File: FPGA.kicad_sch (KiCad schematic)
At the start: 32 parts, among them IC5 AD817ARZ, IC8 N25Q032A11EF840, J3 Conn_01x02, J4 Conn_02x02_Top_Bottom, J5 Conn_01x02, U4 ICE5LP1K-SG48, U9 LTC2451xDDB

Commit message: Begun schematics
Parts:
- removed C20: CC0603_10UF_25V_20%_X5R, Capacitors SMD:CAPC1709X100N, symbol Capacitors SMD:CC0603_10UF_25V_20%_X5R
- removed C21: CC0603_100NF_50V_10%_X7R, Capacitors SMD:CAPC1608X87N, symbol Capacitors SMD:CC0603_100NF_50V_10%_X7R
- removed IC8: N25Q032A11EF840, ICs And Semiconductors SMD:SON127P800X600X100-9N-R515X480, symbol Logic:N25Q032A11EF840
- added D1 (x3): SMBJ3V3, ICs And Semiconductors SMD:DIOM5436X244N, symbol Diodes:SMBJ3V3
- added IC8: MT25QL128ABA1ESE-0SIT, ICs And Semiconductors SMD:SOIC127P790X216-8N, symbol Logic:MT25QL128ABA1ESE-0SIT
- added LD5: LED_LITEON_LTST-C193KGKT-5A, ICs And Semiconductors SMD:LED_LITEON_LTST-C193KGKT-5A, symbol LEDs & Displays:LED_LITEON_LTST-C193KGKT-5A
- added R15: R0603_2K2_1%_0.1W_100PPM, Resistors SMD:RESC1608X55N, symbol Resistors SMD:R0603_2K2_1%_0.1W_100PPM
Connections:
- net +3V3D: now also IC8.8 (VCC), R15.2; no longer C2.1
- net FLASH_MISO: now also IC8.2 (DQ1)
- net FLASH_MOSI: now also IC8.5 (DQ0)
- net GND: now also D1.2 (A), D1.2 (A), D1.2 (A), IC8.4 (VSS)
- net iCE_CDONE: now also D1.1 (C)
- net iCE_SCK: now also IC8.6 (C)
- net iCE_SS_B: now also D1.1 (C)
- net at J3.1 (Pin_1), R25.1: now also D1.1 (C), IC8.1 (~{S})
- net at R24.1: now also IC8.7 (~{HOLD/}DQ3)
- net at R23.1: now also IC8.3 (~{W/}DQ2)
- net +2V5: now reaches U4.24 (VPP_2V5)
- net +2V5: now also C2.1
- net +5VA renamed +5V
- new net: LD5.2 (A), R15.1
- new net FPGA_Alive: LD5.1 (C)
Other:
- moved on the sheet: C2, C20, C21, J3, LD1, R26, U4D

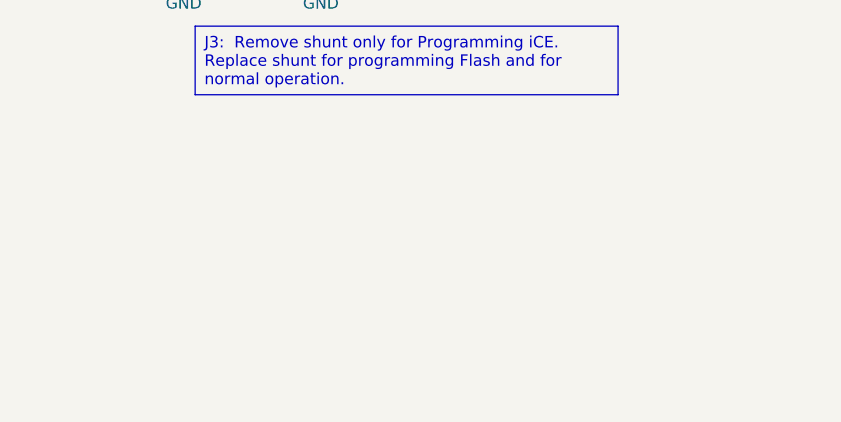
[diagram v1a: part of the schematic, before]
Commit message: Added FPGA oscillator, made FPGA sheet larger
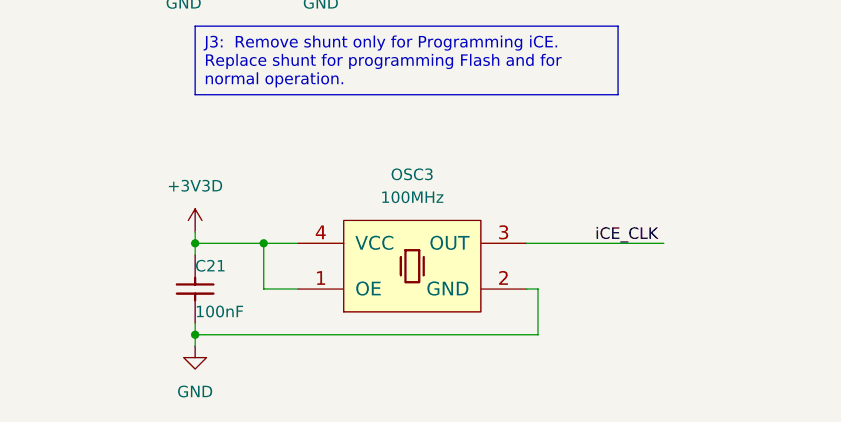
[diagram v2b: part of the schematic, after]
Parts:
- added C21: CC0603_100NF_50V_10%_X7R, Capacitors SMD:CAPC1608X87N, symbol Capacitors SMD:CC0603_100NF_50V_10%_X7R
- added OSC3: OSC_100MHZ_EPSON_SG-8002CAPCB100MHZ, ICs And Semiconductors SMD:OSC_EPSON_SG-8002CA, symbol Crystals & Oscillators:OSC_100MHZ_EPSON_SG-8002CAPCB100MHZ
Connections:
- net +3V3D: now also C21.1, OSC3.1 (OE), OSC3.4 (VCC)
- net GND: now also C21.2, OSC3.2 (GND)
- new net iCE_CLK: OSC3.3 (OUT)

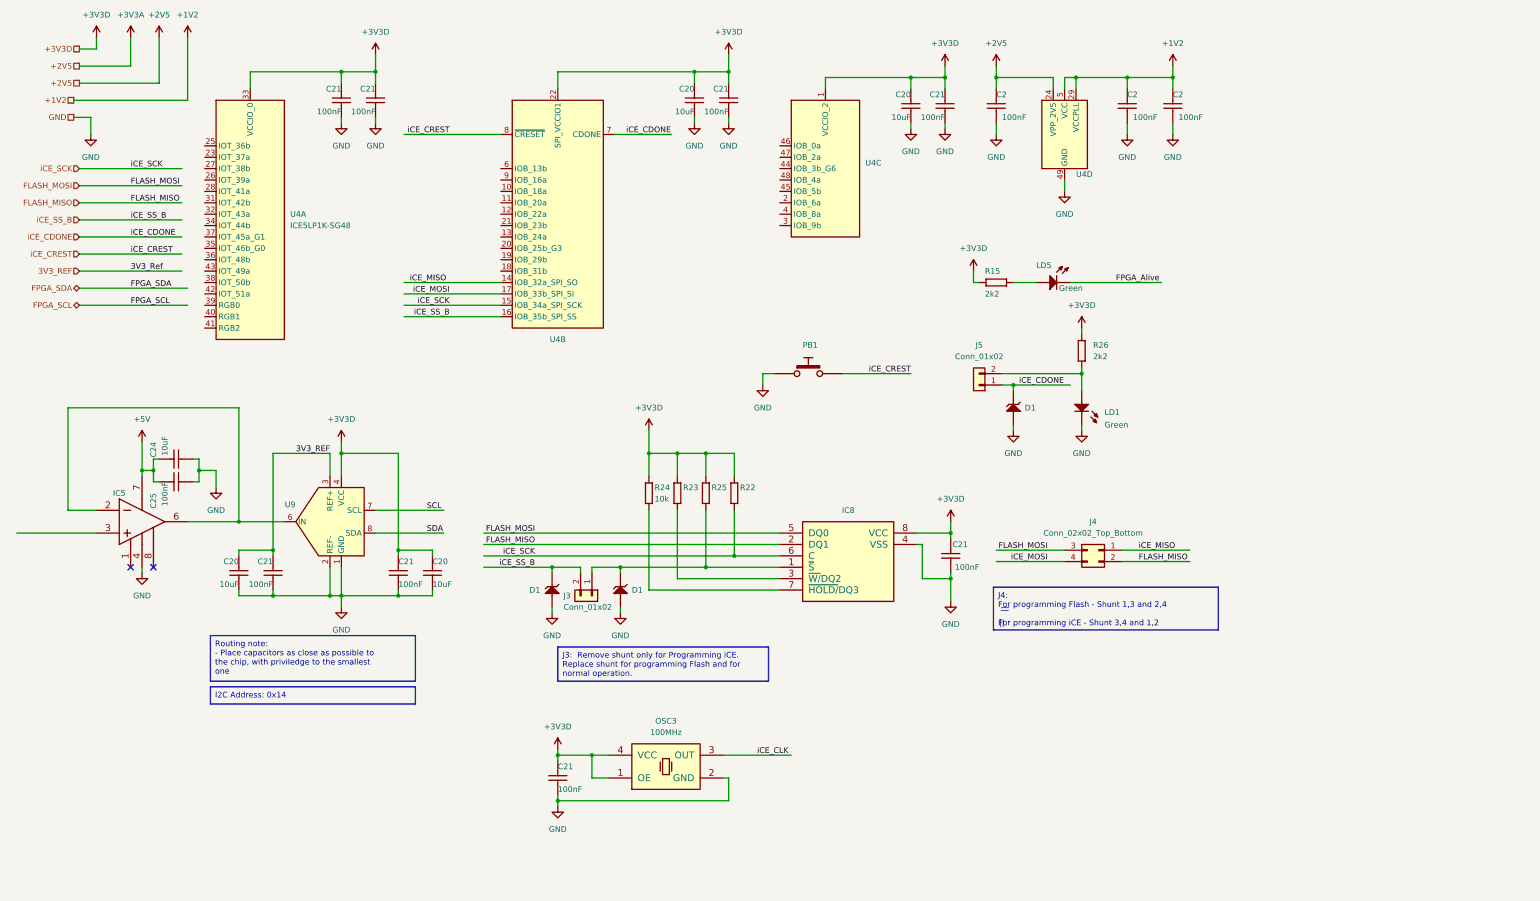
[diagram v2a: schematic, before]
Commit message: Connected FPGA to Accurate, added Atsam, fixed some Accurate connections
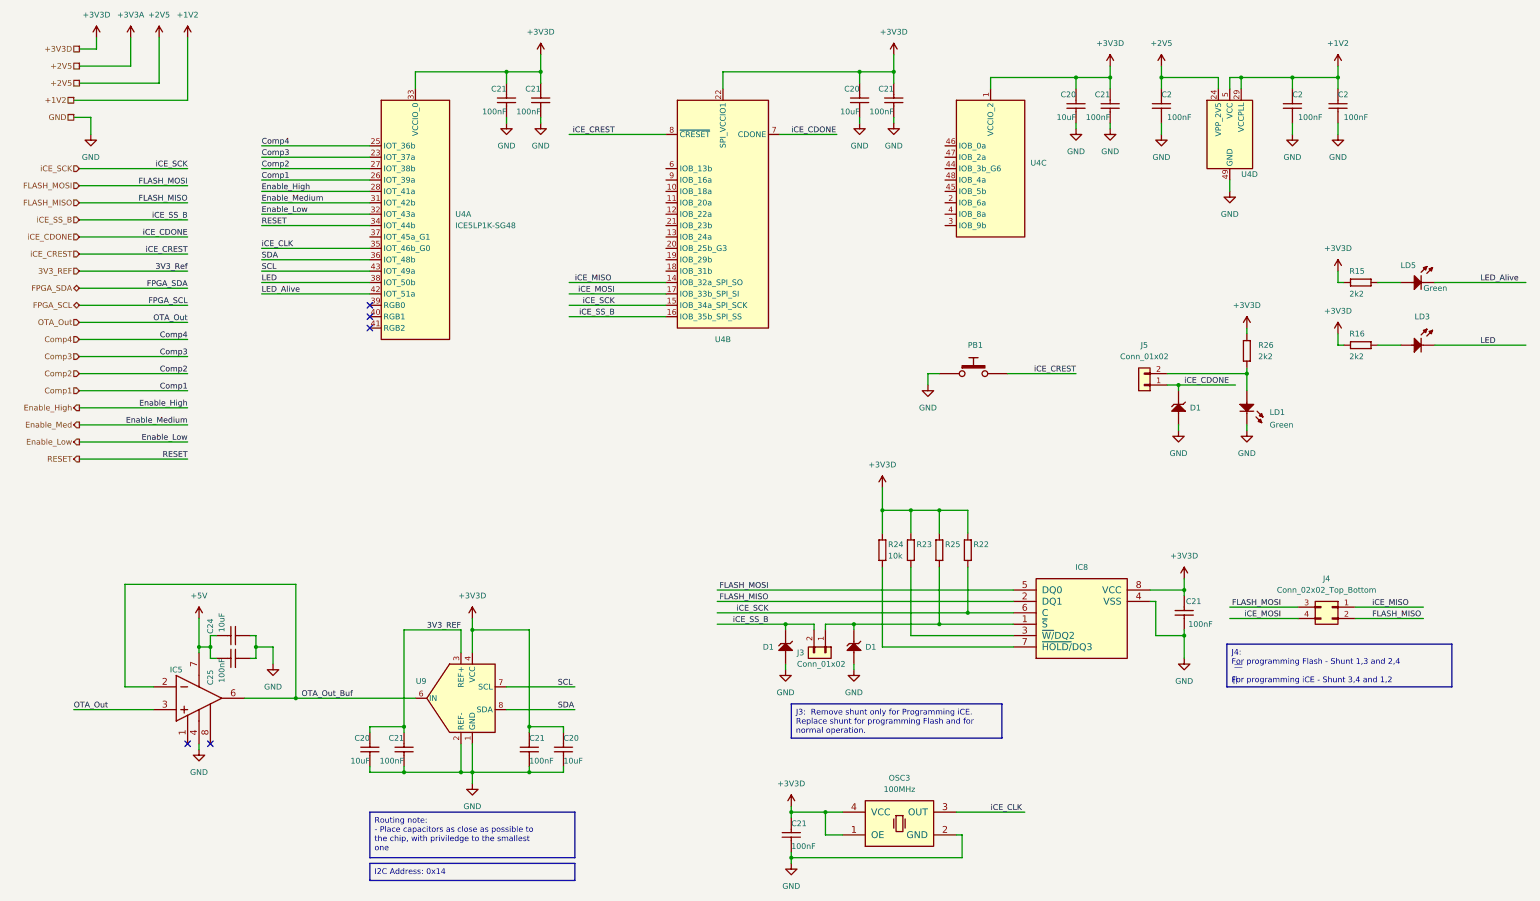
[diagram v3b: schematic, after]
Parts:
- added LD3: LED_LITEON_LTST-C193KSKT-5A, ICs And Semiconductors SMD:LED_LITEON_LTST-C193KSKT-5A, symbol LEDs & Displays:LED_LITEON_LTST-C193KSKT-5A
- added R16: R0603_2K2_1%_0.1W_100PPM, Resistors SMD:RESC1608X55N, symbol Resistors SMD:R0603_2K2_1%_0.1W_100PPM
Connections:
- net FPGA_Alive is gone; now on net LED_Alive: LD5.1 (C)
- net +3V3D: now also R16.2
- net SCL: now also U4.43 (IOT_49a)
- net SDA: now also U4.36 (IOT_48b)
- net iCE_CLK: now also U4.35 (IOT_46b_G0)
- net OTA_Out_Buf: now reaches IC5.2 (IN-), IC5.6 (OUT), U9.6 (IN)
- net Comp3: now reaches U4.23 (IOT_37a)
- net Comp4: now reaches U4.25 (IOT_36b)
- net Comp1: now reaches U4.26 (IOT_39a)
- net Comp2: now reaches U4.27 (IOT_38b)
- net Enable_High: now reaches U4.28 (IOT_41a)
- net Enable_Med: now reaches U4.31 (IOT_42b)
- net Enable_Low: now reaches U4.32 (IOT_43a)
- net RESET: now reaches U4.34 (IOT_44b)
- net LED: now reaches U4.38 (IOT_50b)
- net LED: now also LD3.1 (C)
- net LED_Alive: now reaches U4.42 (IOT_51a)
- net OTA_Out: now reaches IC5.3 (IN+)
- new net: LD3.2 (A), R16.1
- no-connect marks 2 -> 5
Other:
- moved on the sheet: C2, C20, C21, C24, C25, D1, IC5, IC8, J3, J4, J5, LD1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

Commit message: Made MCU schematic, made root schematic, adding ESD diodes, fixed  EDR errors
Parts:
- added C21 (x2): CC0603_100NF_50V_10%_X7R, Capacitors SMD:CAPC1608X87N, symbol Capacitors SMD:CC0603_100NF_50V_10%_X7R
- added D6: PESD3V3L5UY, Package_TO_SOT_SMD:SOT-363_SC-70-6, symbol Power_Protection:PESD3V3L5UY
- added J13, J8: Conn_02x06_Top_Bottom, symbol Connector_Generic:Conn_02x06_Top_Bottom
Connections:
- net SCL is gone; now on net FPGA_SCL: U4.43 (IOT_49a), U9.7 (SCL)
- net SDA is gone; now on net FPGA_SDA: U4.36 (IOT_48b), U9.8 (SDA)
- net +3V3D: now also C21.1, C21.1, J13.12 (Pin_12), J13.6 (Pin_6), J8.12 (Pin_12), J8.6 (Pin_6)
- net GND: now also C21.2, C21.2, D6.2 (A), J13.11 (Pin_11), J13.5 (Pin_5), J8.11 (Pin_11), J8.5 (Pin_5)
- net iCE_MISO: now also D6.5 (K4)
- net iCE_MOSI: now also D6.3 (K2)
- net FPGA_CLK: now reaches U4.37 (IOT_45a_G1)
- net IOB_18: now reaches U4.10 (IOB_18a)
- net IOB_18: now also J13.3 (Pin_3)
- net IOB_20: now reaches U4.11 (IOB_20a)
- net IOB_20: now also J13.4 (Pin_4)
- net IOB_22: now reaches U4.12 (IOB_22a)
- net IOB_22: now also J13.7 (Pin_7)
- net IOB_24: now reaches U4.13 (IOB_24a)
- net IOB_24: now also J13.9 (Pin_9)
- net MCU_SCL: now reaches U4.18 (IOB_31b)
- net MCU_SDA: now reaches U4.19 (IOB_29b)
- net IOB_25: now reaches U4.20 (IOB_25b_G3)
- net IOB_25: now also J13.10 (Pin_10)
- net IOB_23: now reaches U4.21 (IOB_23b)
- net IOB_23: now also J13.8 (Pin_8)
- net IOB_13: now reaches U4.6 (IOB_13b)
- net IOB_13: now also J13.1 (Pin_1)
- net IOB_16: now reaches U4.9 (IOB_16a)
- net IOB_16: now also J13.2 (Pin_2)
- net IOB_6: now reaches U4.2 (IOB_6a)
- net IOB_6: now also J8.8 (Pin_8)
- net IOB_9: now reaches U4.3 (IOB_9b)
- net IOB_9: now also J8.10 (Pin_10)
- net IOB_8: now reaches U4.4 (IOB_8a)
- net IOB_8: now also J8.9 (Pin_9)
- net IOB_3: now reaches U4.44 (IOB_3b_G6)
- net IOB_3: now also J8.3 (Pin_3)
- net IOB_5: now reaches U4.45 (IOB_5b)
- net IOB_5: now also J8.7 (Pin_7)
- net IOB_0: now reaches U4.46 (IOB_0a)
- net IOB_0: now also J8.1 (Pin_1)
- net IOB_2: now reaches U4.47 (IOB_2a)
- net IOB_2: now also J8.2 (Pin_2)
- net IOB_4: now reaches U4.48 (IOB_4a)
- net IOB_4: now also J8.4 (Pin_4)
- net Enable_High renamed Enable.High
- net Enable_Low renamed Enable.Low
- net Enable_Med renamed Enable.Medium
- net FLASH_MISO renamed ADBUS2
- net ADBUS2: now also D6.6 (K5)
- net FLASH_MOSI renamed ADBUS1
- net ADBUS1: now also D6.4 (K3)
- net iCE_CDONE renamed ADBUS6
- net iCE_CREST renamed ADBUS7
- net iCE_SCK renamed ADBUS0
- net iCE_SS_B renamed ADBUS4
- no-connect marks 5 -> 6
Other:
- note added: "CDONE Status LED"
- note added: "Flash"
- note added: "Flash/iCE Header"
- note added: "Inputs"
- note added: "LEDs"
- note added: "OTA ADC"
- note added: "Oscillator"
- note added: "Outputs"
- note added: "PMOD Connectors"
- note added: "Power Ports"
- note added: "Reset"
- note added: "iCE40 Ultra FPGA"
- moved on the sheet: C2, C20, C21, C24, C25, D1, IC5, IC8, J3, J4, J5, LD1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
